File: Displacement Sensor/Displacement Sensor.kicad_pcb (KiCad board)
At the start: 2 copper layers, 56.8 x 46 mm, 21 parts, among them J1 DTF13-6P, U3 MCP2515-I, U4 TJA1050DRG, X1 8MHz

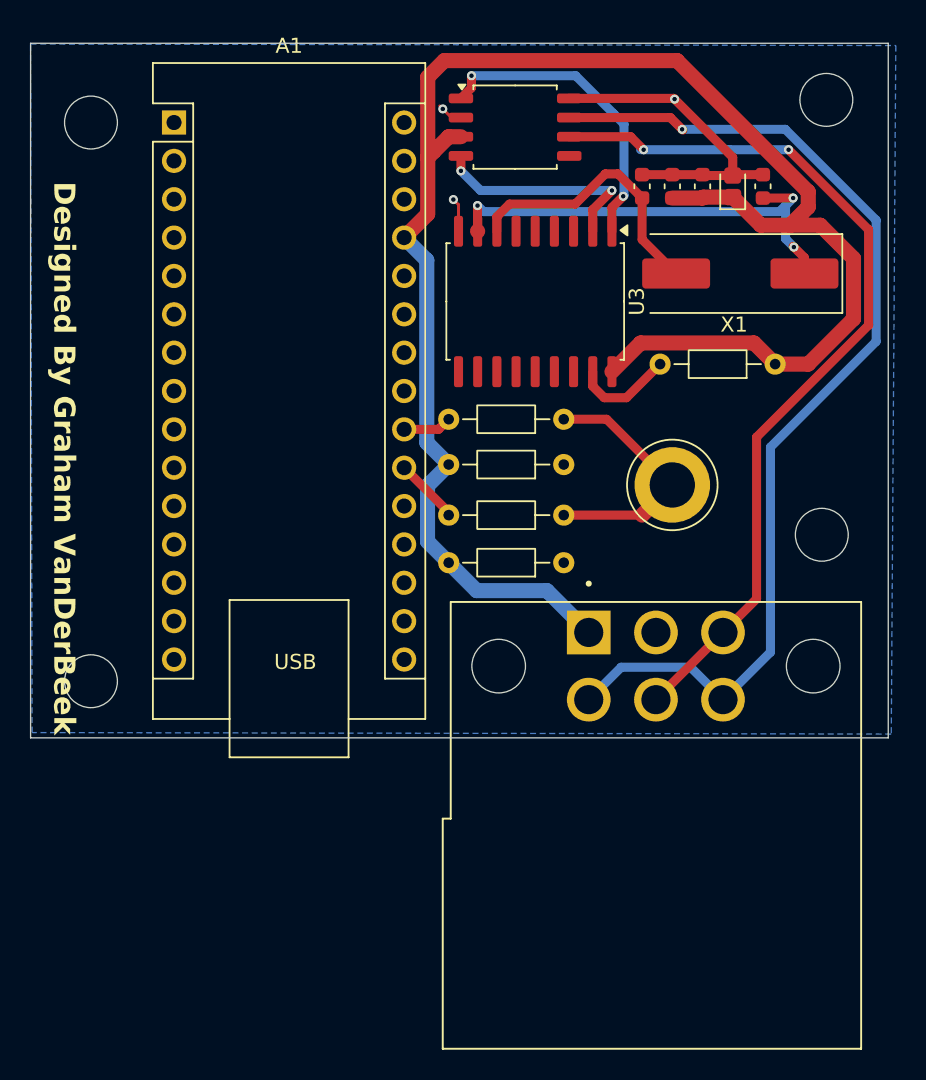
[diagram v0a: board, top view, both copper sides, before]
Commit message: Added Fiducial Points
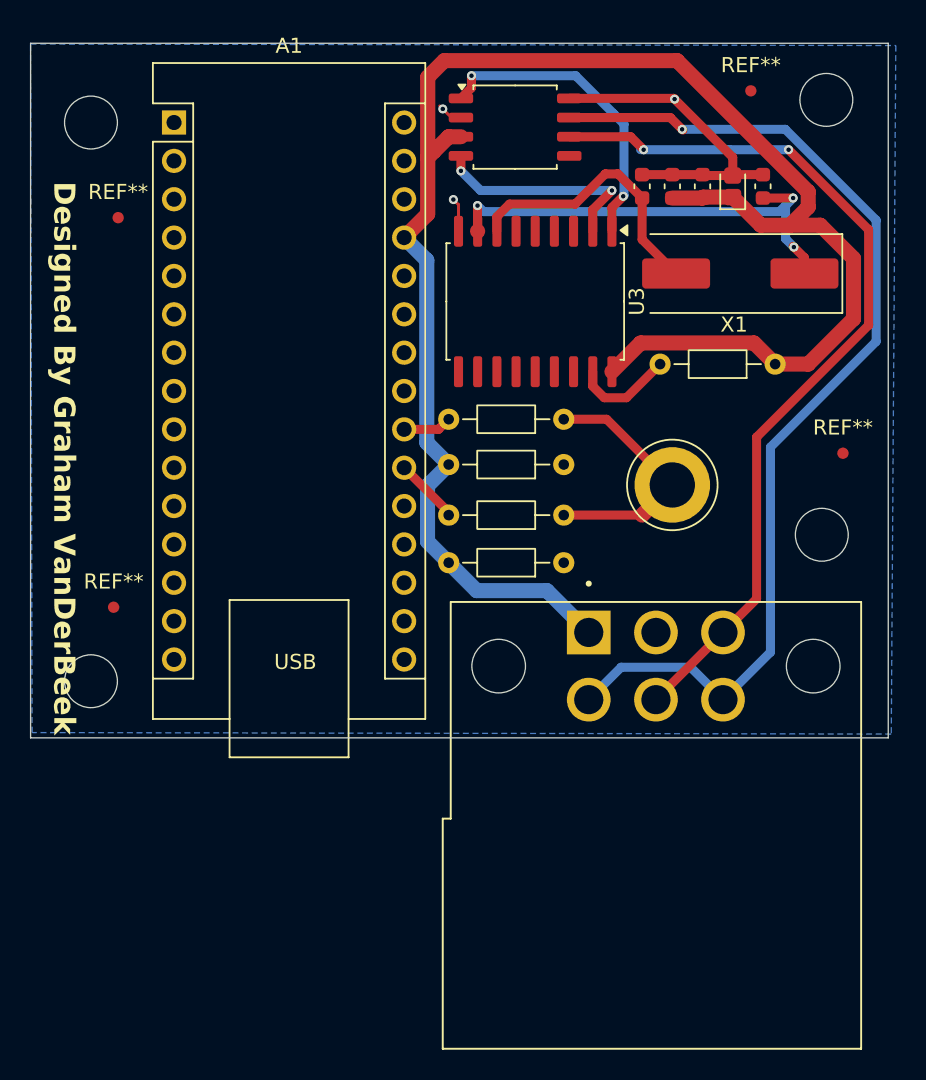
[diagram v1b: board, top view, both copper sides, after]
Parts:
- added REF**: Fiducial_0.75mm_Mask1.5mm, Fiducial:Fiducial_0.75mm_Mask1.5mm, F.Cu at (116.3, 105.9)
- added REF**: Fiducial_0.75mm_Mask1.5mm, Fiducial:Fiducial_0.75mm_Mask1.5mm, F.Cu at (110.2, 81.9)
- added REF**: Fiducial_0.75mm_Mask1.5mm, Fiducial:Fiducial_0.75mm_Mask1.5mm, F.Cu at (68.3, 90.3)
- added REF**: Fiducial_0.75mm_Mask1.5mm, Fiducial:Fiducial_0.75mm_Mask1.5mm, F.Cu at (68.0, 116.1)

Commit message: Updated Again
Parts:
- renumbered C11 to C1, C12 to C2, C13 to C3, C14 to C4, C15 to C5, R13 to R3, U4 to U1, U3 to U2
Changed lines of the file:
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@@
 	(net 28 "unconnected-(A1-A7-Pad26)")
 	(net 29 "unconnected-(A1-3V3-Pad17)")
-	(net 30 "Net-(U3-OSC2)")
-	(net 31 "Net-(U3-OSC1)")
+	(net 30 "Net-(U2-OSC2)")
+	(net 31 "Net-(U2-OSC1)")
 	(net 32 "CGND")
-	(net 33 "Net-(U3-~{RESET})")
-	(net 34 "unconnected-(U3-~{TX0RTS}-Pad4)")
+	(net 33 "Net-(U2-~{RESET})")
+	(net 34 "Net-(U1-RXD)")
 	(net 35 "SO")
 	(net 36 "SI")
-	(net 37 "Net-(U3-RXCAN)")
-	(net 38 "unconnected-(U3-~{TX2RTS}-Pad6)")
-	(net 39 "Net-(U3-TXCAN)")
+	(net 37 "Net-(U1-TXD)")
+	(net 38 "unconnected-(U1-SPLIT-Pad5)")
+	(net 39 "unconnected-(U2-~{TX0RTS}-Pad4)")
 	(net 40 "CS")
-	(net 41 "unconnected-(U3-~{RX1BF}-Pad10)")
-	(net 42 "unconnected-(U3-~{INT}-Pad12)")
+	(net 41 "unconnected-(U2-~{TX2RTS}-Pad6)")
+	(net 42 "unconnected-(U2-~{RX1BF}-Pad10)")
 	(net 43 "SCK")
-	(net 44 "unconnected-(U3-~{TX1RTS}-Pad5)")
-	(net 45 "unconnected-(U3-CLKOUT{slash}SOF-Pad3)")
-	(net 46 "unconnected-(U3-~{RX0BF}-Pad11)")
+	(net 44 "unconnected-(U2-~{INT}-Pad12)")
+	(net 45 "unconnected-(U2-~{TX1RTS}-Pad5)")
+	(net 46 "unconnected-(U2-CLKOUT{slash}SOF-Pad3)")
 	(net 47 "High")
 	(net 48 "Low")
-	(net 49 "unconnected-(U4-SPLIT-Pad5)")
+	(net 49 "unconnected-(U2-~{RX0BF}-Pad11)")
 	(footprint "Capacitor_SMD:C_0603_1608Metric"
 		(layer "F.Cu")
@@
 		(descr "Capacitor SMD 0603 (1608 Metric), square (rectangular) end terminal, IPC-7351 nominal, (Body size source: IPC-SM-782 page 76, https://www.pcb-3d.com/wordpress/wp-content/uploads/ipc-sm-782a_amendment_1_and_2.pdf), generated with kicad-footprint-generator")
 		(tags "capacitor")
-		(property "Reference" "C14"
+		(property "Reference" "C4"
 			(at -2.475 0 180)
 			(layer "F.SilkS")
@@
 			(layers "F.Cu" "F.Mask" "F.Paste")
 			(roundrect_rratio 0.25)
-			(net 31 "Net-(U3-OSC1)")
+			(net 31 "Net-(U2-OSC1)")
 			(pinfunction "1")
 			(pintype "passive")
@@
 		(descr "Capacitor SMD 0603 (1608 Metric), square (rectangular) end terminal, IPC-7351 nominal, (Body size source: IPC-SM-782 page 76, https://www.pcb-3d.com/wordpress/wp-content/uploads/ipc-sm-782a_amendment_1_and_2.pdf), generated with kicad-footprint-generator")
 		(tags "capacitor")
-		(property "Reference" "C12"
+		(property "Reference" "C2"
 			(at 3.875 0.2 180)
 			(layer "F.SilkS")
@@
 		(descr "SOIC, 8 Pin (JEITA/EIAJ ED-7311-19 variation 08-001-BBA and Atmel/Microchip, 208 mils width, https://www.jeita.or.jp/japanese/standard/book/ED-7311-19/#target/page_no=21, https://ww1.microchip.com/downloads/en/DeviceDoc/20005045C.pdf#page=23, https://ww1.microchip.com/downloads/en/DeviceDoc/doc2535.pdf#page=162), generated with kicad-footprint-generator ipc_gullwing_generator.py")
 		(tags "SOIC SO P-SOP SOP SOP-8 SO SO-8 8S2 S2AE/F K04-056 CASE-751BE SO8W 8-Pin-SOIC PSA W8-2 W8-4 W8MS-1 FPT-8P-M08")
-		(property "Reference" "U4"
+		(property "Reference" "U1"
 			(at 0 1.635 0)
 			(layer "F.SilkS")
@@
 			(layers "F.Cu" "F.Mask" "F.Paste")
 			(roundrect_rratio 0.25)
-			(net 39 "Net-(U3-TXCAN)")
+			(net 37 "Net-(U1-TXD)")
 			(pinfunction "TXD")
 			(pintype "passive")
@@
 			(layers "F.Cu" "F.Mask" "F.Paste")
 			(roundrect_rratio 0.25)
-			(net 37 "Net-(U3-RXCAN)")
+			(net 34 "Net-(U1-RXD)")
 			(pinfunction "RXD")
 			(pintype "passive")
@@
 			(layers "F.Cu" "F.Mask" "F.Paste")
 			(roundrect_rratio 0.25)
-			(net 49 "unconnected-(U4-SPLIT-Pad5)")
+			(net 38 "unconnected-(U1-SPLIT-Pad5)")
 			(pinfunction "SPLIT")
 			(pintype "passive+no_connect")
@@
 			(layers "F.Cu" "F.Mask" "F.Paste")
 			(roundrect_rratio 0.125)
-			(net 31 "Net-(U3-OSC1)")
+			(net 31 "Net-(U2-OSC1)")
 			(pinfunction "1")
 			(pintype "passive")
@@
 			(layers "F.Cu" "F.Mask" "F.Paste")
 			(roundrect_rratio 0.125)
-			(net 30 "Net-(U3-OSC2)")
+			(net 30 "Net-(U2-OSC2)")
 			(pinfunction "2")
 			(pintype "passive")
@@
 		(descr "Capacitor SMD 0603 (1608 Metric), square (rectangular) end terminal, IPC-7351 nominal, (Body size source: IPC-SM-782 page 76, https://www.pcb-3d.com/wordpress/wp-content/uploads/ipc-sm-782a_amendment_1_and_2.pdf), generated with kicad-footprint-generator")
 		(tags "capacitor")
-		(property "Reference" "C15"
+		(property "Reference" "C5"
 			(at -2.5 0 180)
 			(layer "F.SilkS")
@@
 		(descr "SOIC, 18 Pin (JEDEC MS-013AB, https://www.analog.com/media/en/package-pcb-resources/package/33254132129439rw_18.pdf), generated with kicad-footprint-generator ipc_gullwing_generator.py")
 		(tags "SOIC SO")
-		(property "Reference" "U3"
+		(property "Reference" "U2"
 			(at 0 -6.73 90)
 			(layer "F.SilkS")
@@
 			(layers "F.Cu" "F.Mask" "F.Paste")
 			(roundrect_rratio 0.25)
-			(net 39 "Net-(U3-TXCAN)")
+			(net 37 "Net-(U1-TXD)")
 			(pinfunction "TXCAN")
 			(pintype "passive")
@@
 			(layers "F.Cu" "F.Mask" "F.Paste")
 			(roundrect_rratio 0.25)
-			(net 37 "Net-(U3-RXCAN)")
+			(net 34 "Net-(U1-RXD)")
 			(pinfunction "RXCAN")
 			(pintype "passive")
@@
 			(layers "F.Cu" "F.Mask" "F.Paste")
 			(roundrect_rratio 0.25)
-			(net 45 "unconnected-(U3-CLKOUT{slash}SOF-Pad3)")
+			(net 46 "unconnected-(U2-CLKOUT{slash}SOF-Pad3)")
 			(pinfunction "CLKOUT/SOF")
 			(pintype "passive+no_connect")
@@
 			(layers "F.Cu" "F.Mask" "F.Paste")
 			(roundrect_rratio 0.25)
-			(net 34 "unconnected-(U3-~{TX0RTS}-Pad4)")
+			(net 39 "unconnected-(U2-~{TX0RTS}-Pad4)")
 			(pinfunction "~{TX0RTS}")
 			(pintype "passive+no_connect")
@@
 			(layers "F.Cu" "F.Mask" "F.Paste")
 			(roundrect_rratio 0.25)
-			(net 44 "unconnected-(U3-~{TX1RTS}-Pad5)")
+			(net 45 "unconnected-(U2-~{TX1RTS}-Pad5)")
 			(pinfunction "~{TX1RTS}")
 			(pintype "passive+no_connect")
@@
 			(layers "F.Cu" "F.Mask" "F.Paste")
 			(roundrect_rratio 0.25)
-			(net 38 "unconnected-(U3-~{TX2RTS}-Pad6)")
+			(net 41 "unconnected-(U2-~{TX2RTS}-Pad6)")
 			(pinfunction "~{TX2RTS}")
 			(pintype "passive+no_connect")
@@
 			(layers "F.Cu" "F.Mask" "F.Paste")
 			(roundrect_rratio 0.25)
-			(net 30 "Net-(U3-OSC2)")
+			(net 30 "Net-(U2-OSC2)")
 			(pinfunction "OSC2")
 			(pintype "passive")
@@
 			(layers "F.Cu" "F.Mask" "F.Paste")
 			(roundrect_rratio 0.25)
-			(net 31 "Net-(U3-OSC1)")
+			(net 31 "Net-(U2-OSC1)")
 			(pinfunction "OSC1")
 			(pintype "passive")
@@
 			(layers "F.Cu" "F.Mask" "F.Paste")
 			(roundrect_rratio 0.25)
-			(net 41 "unconnected-(U3-~{RX1BF}-Pad10)")
+			(net 42 "unconnected-(U2-~{RX1BF}-Pad10)")
 			(pinfunction "~{RX1BF}")
 			(pintype "passive+no_connect")
@@
 			(layers "F.Cu" "F.Mask" "F.Paste")
 			(roundrect_rratio 0.25)
-			(net 46 "unconnected-(U3-~{RX0BF}-Pad11)")
+			(net 49 "unconnected-(U2-~{RX0BF}-Pad11)")
 			(pinfunction "~{RX0BF}")
 			(pintype "passive+no_connect")
@@
 			(layers "F.Cu" "F.Mask" "F.Paste")
 			(roundrect_rratio 0.25)
-			(net 42 "unconnected-(U3-~{INT}-Pad12)")
+			(net 44 "unconnected-(U2-~{INT}-Pad12)")
 			(pinfunction "~{INT}")
 			(pintype "passive+no_connect")
@@
 			(layers "F.Cu" "F.Mask" "F.Paste")
 			(roundrect_rratio 0.25)
-			(net 33 "Net-(U3-~{RESET})")
+			(net 33 "Net-(U2-~{RESET})")
 			(pinfunction "~{RESET}")
 			(pintype "passive")
@@
 		(descr "Capacitor SMD 0603 (1608 Metric), square (rectangular) end terminal, IPC-7351 nominal, (Body size source: IPC-SM-782 page 76, https://www.pcb-3d.com/wordpress/wp-content/uploads/ipc-sm-782a_amendment_1_and_2.pdf), generated with kicad-footprint-generator")
 		(tags "capacitor")
-		(property "Reference" "C13"
+		(property "Reference" "C3"
 			(at 2.125 -1.3 180)
 			(layer "F.SilkS")
@@
 			(layers "F.Cu" "F.Mask" "F.Paste")
 			(roundrect_rratio 0.25)
-			(net 30 "Net-(U3-OSC2)")
+			(net 30 "Net-(U2-OSC2)")
 			(pinfunction "1")
 			(pintype "passive")
@@
 		(descr "Tantalum Capacitor SMD AVX-J (1608-08 Metric), IPC-7352 nominal, (Body size from: https://www.vishay.com/docs/48064/_t58_vmn_pt0471_1601.pdf), generated with kicad-footprint-generator")
 		(tags "capacitor tantalum")
-		(property "Reference" "C11"
+		(property "Reference" "C1"
 			(at 3.225 -0.3 180)
 			(layer "F.SilkS")
@@
 		(descr "Resistor, Axial_DIN0204 series, Axial, Horizontal, pin pitch=7.62mm, 0.167W, length*diameter=3.6*1.6mm^2, http://cdn-reichelt.de/documents/datenblatt/B400/1_4W%23YAG.pdf")
 		(tags "Resistor Axial_DIN0204 series Axial Horizontal pin pitch 7.62mm 0.167W length 3.6mm diameter 1.6mm")
-		(property "Reference" "R13"
+		(property "Reference" "R3"
 			(at 3.81 -1.92 0)
 			(layer "F.SilkS")
@@
 			(layers "*.Cu" "*.Mask")
 			(remove_unused_layers no)
-			(net 33 "Net-(U3-~{RESET})")
+			(net 33 "Net-(U2-~{RESET})")
 			(pintype "passive")
 		)
@@
 		(width 0.6)
 		(layer "F.Cu")
-		(net 37)
+		(net 34)
 	)
 	(segment
@@
 		(width 0.6)
 		(layer "F.Cu")
-		(net 37)
+		(net 34)
 	)
 	(segment
@@
 		(width 0.6)
 		(layer "F.Cu")
-		(net 37)
+		(net 34)
 	)
 	(via
@@
 		(drill 0.3)
 		(layers "F.Cu" "B.Cu")
-		(net 37)
+		(net 34)
 	)
 	(via
@@
 		(drill 0.3)
 		(layers "F.Cu" "B.Cu")
-		(net 37)
+		(net 34)
 	)
 	(segment
@@
 		(width 0.6)
 		(layer "B.Cu")
-		(net 37)
+		(net 34)
 	)
 	(segment
@@
 		(width 0.6)
 		(layer "B.Cu")
-		(net 37)
+		(net 34)
 	)
 	(segment
@@
 		(width 0.6)
 		(layer "F.Cu")
-		(net 39)
+		(net 37)
 	)
 	(segment
@@
 		(width 0.6)
 		(layer "F.Cu")
-		(net 39)
+		(net 37)
 	)
 	(segment
@@
 		(width 0.6)
 		(layer "F.Cu")
-		(net 39)
+		(net 37)
 	)
 	(segment
@@
 		(width 0.6)
 		(layer "F.Cu")
-		(net 39)
+		(net 37)
 	)
 	(via
@@
 		(drill 0.3)
 		(layers "F.Cu" "B.Cu")
-		(net 39)
+		(net 37)
 	)
 	(via
@@
 		(drill 0.3)
 		(layers "F.Cu" "B.Cu")
-		(net 39)
+		(net 37)
 	)
 	(segment
@@
 		(width 0.6)
 		(layer "B.Cu")
-		(net 39)
+		(net 37)
 	)
 	(segment
@@
 		(width 0.6)
 		(layer "B.Cu")
-		(net 39)
+		(net 37)
 	)
 	(segment
@@
 		(width 0.6)
 		(layer "B.Cu")
-		(net 39)
+		(net 37)
 	)
 	(segment
@@
 		(width 0.6)
 		(layer "B.Cu")
-		(net 39)
+		(net 37)
 	)
 	(segment
@@
 		(width 0.6)
 		(layer "B.Cu")
-		(net 39)
+		(net 37)
 	)
 	(segment
